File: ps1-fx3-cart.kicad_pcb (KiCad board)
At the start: 4 copper layers, 86.4 x 63.5 mm, 98 parts, among them J1 PIO, J2 ZX360D-B-10P, J3 JTAG, J4 UART, Q1 2N7002, SW1 RESET, U1 CYUSB3014-BZXI, U2 S29AL016J70TFI020, U3 24LC1025-I/SN, U4 24LC1025-I/SN, U5 TLV62569DBVR, Y1 19.2MHz

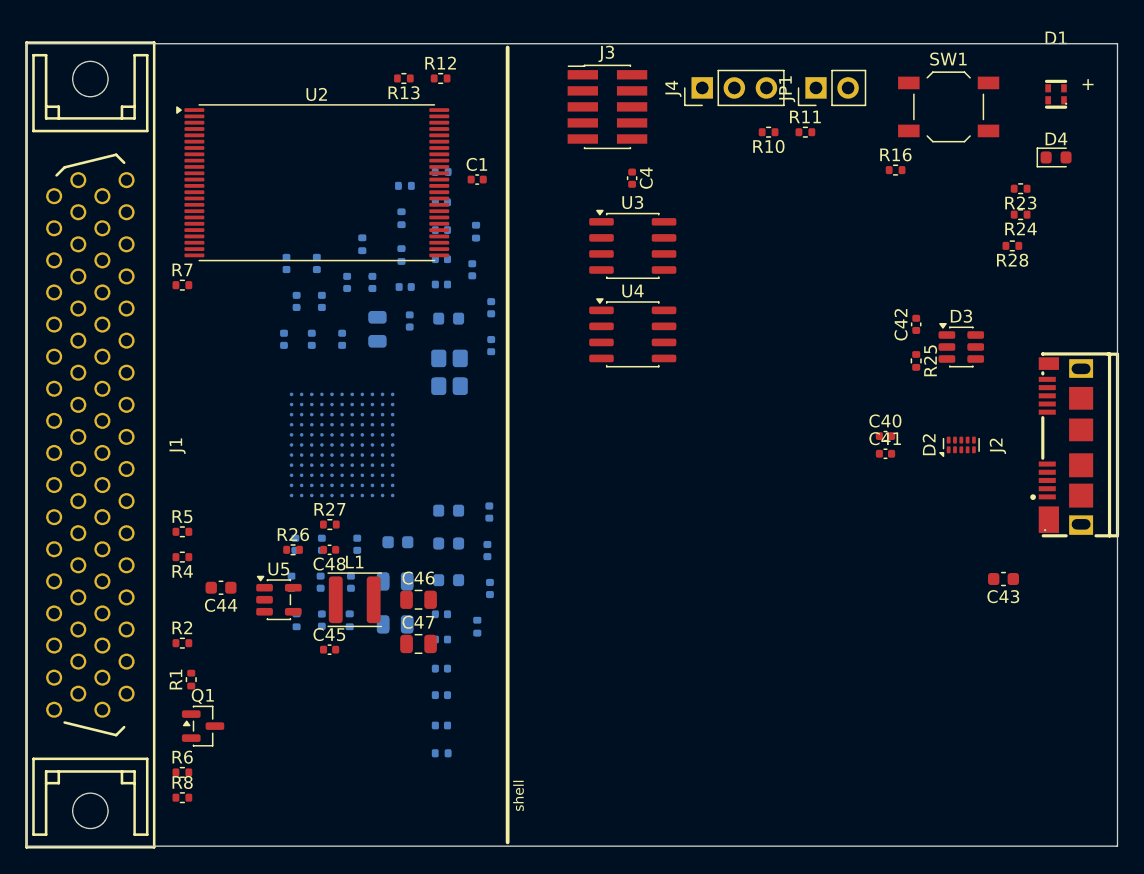
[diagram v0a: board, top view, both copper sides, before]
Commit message: Route planes, supplies, USB, crystal and I2C; J1 nets left open
route_usb.py builds In1 GND and In2 +3V3 with a +1V2 island under the FX3, then
routes the SS and HS pairs on the 90 ohm class (skew 0.000/0.015/0.000 mm).
fanout.py and p2p_route.py then do the planes, buck, crystal and EEPROM.
DRC: copper 0, unconnected 348 -> 105 (74 on J1, 31 JTAG/UART/LED/PMODE/reset).
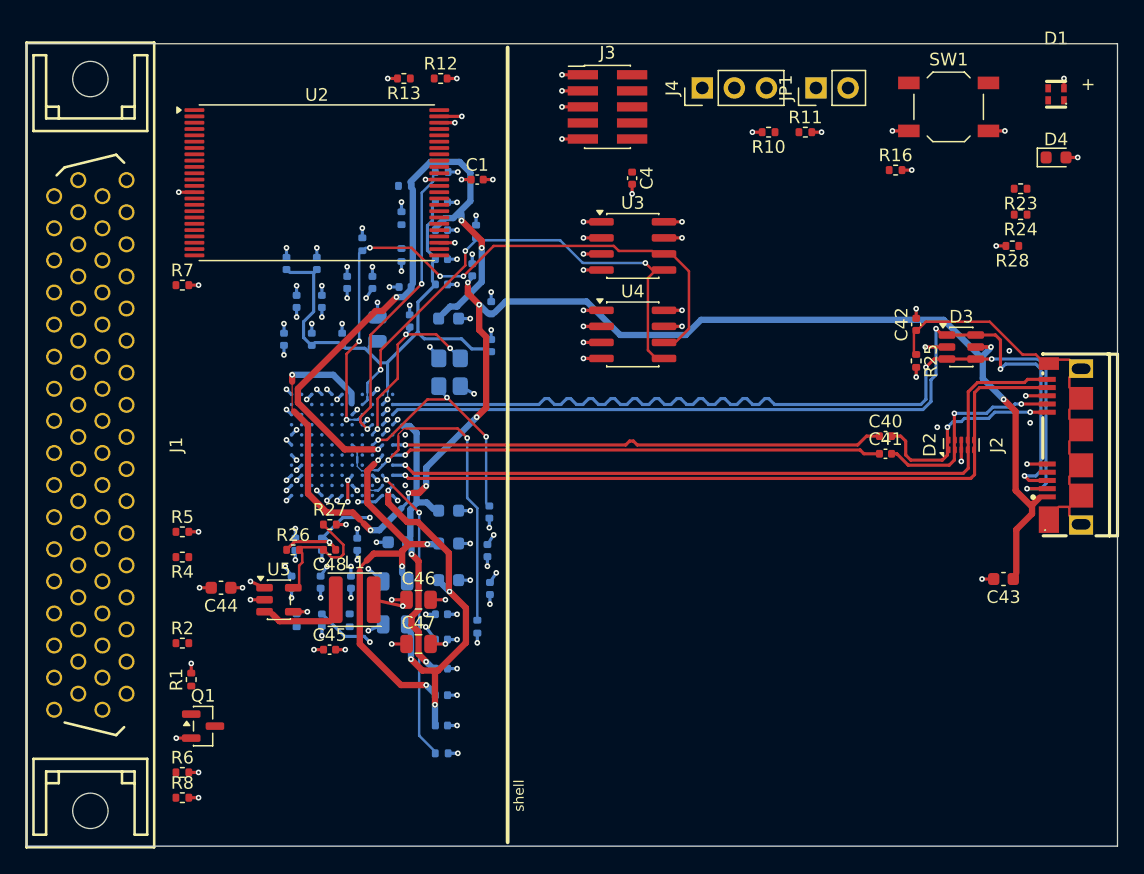
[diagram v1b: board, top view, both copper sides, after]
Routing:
- net VBUS: track 0.00 -> 111.8 mm, vias 0 -> 9
- net GND: track 0.00 -> 88.0 mm, vias 0 -> 100
- net USB3_DM: track 0.00 -> 71.7 mm, vias 0 -> 3
- net USB3_DP: track 0.00 -> 71.7 mm, vias 0 -> 3
- net +1V2: track 0.00 -> 62.6 mm, vias 0 -> 19
- net USB3_RXP: track 0.00 -> 58.7 mm, vias 0 -> 1
- net USB3_RXN: track 0.00 -> 58.7 mm, vias 0 -> 1
- net FX3_CVDDQ: track 0.00 -> 50.7 mm, vias 0 -> 4
- net I2C_SCL: track 0.00 -> 47.3 mm, vias 0 -> 5
- net +3V3: track 0.00 -> 41.0 mm, vias 0 -> 44
- net USB3_TXN_C: track 0.00 -> 39.1 mm, vias 0 -> 1
- net USB3_TXP_C: track 0.00 -> 38.8 mm, vias 0 -> 1
- net I2C_SDA: track 0.00 -> 38.0 mm, vias 0 -> 3
- net FX3_U3TX: track 0.00 -> 30.2 mm, vias 0 -> 4
- net FX3_FSLC: track 0.00 -> 30.0 mm, vias 0 -> 2
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- added copper zone on In2.Cu, net +1V2
- added copper zone on In2.Cu, net +3V3
- added copper zone on In1.Cu, net GND
- added copper zone on In2.Cu, net GND
